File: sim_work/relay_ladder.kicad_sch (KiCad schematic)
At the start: 26 parts, among them Q1 2N3904, Q2 2N3904, Q3 2N3904, Q4 2N3904, SW1 K1, SW2 K2, SW3 K3, SW4 K4

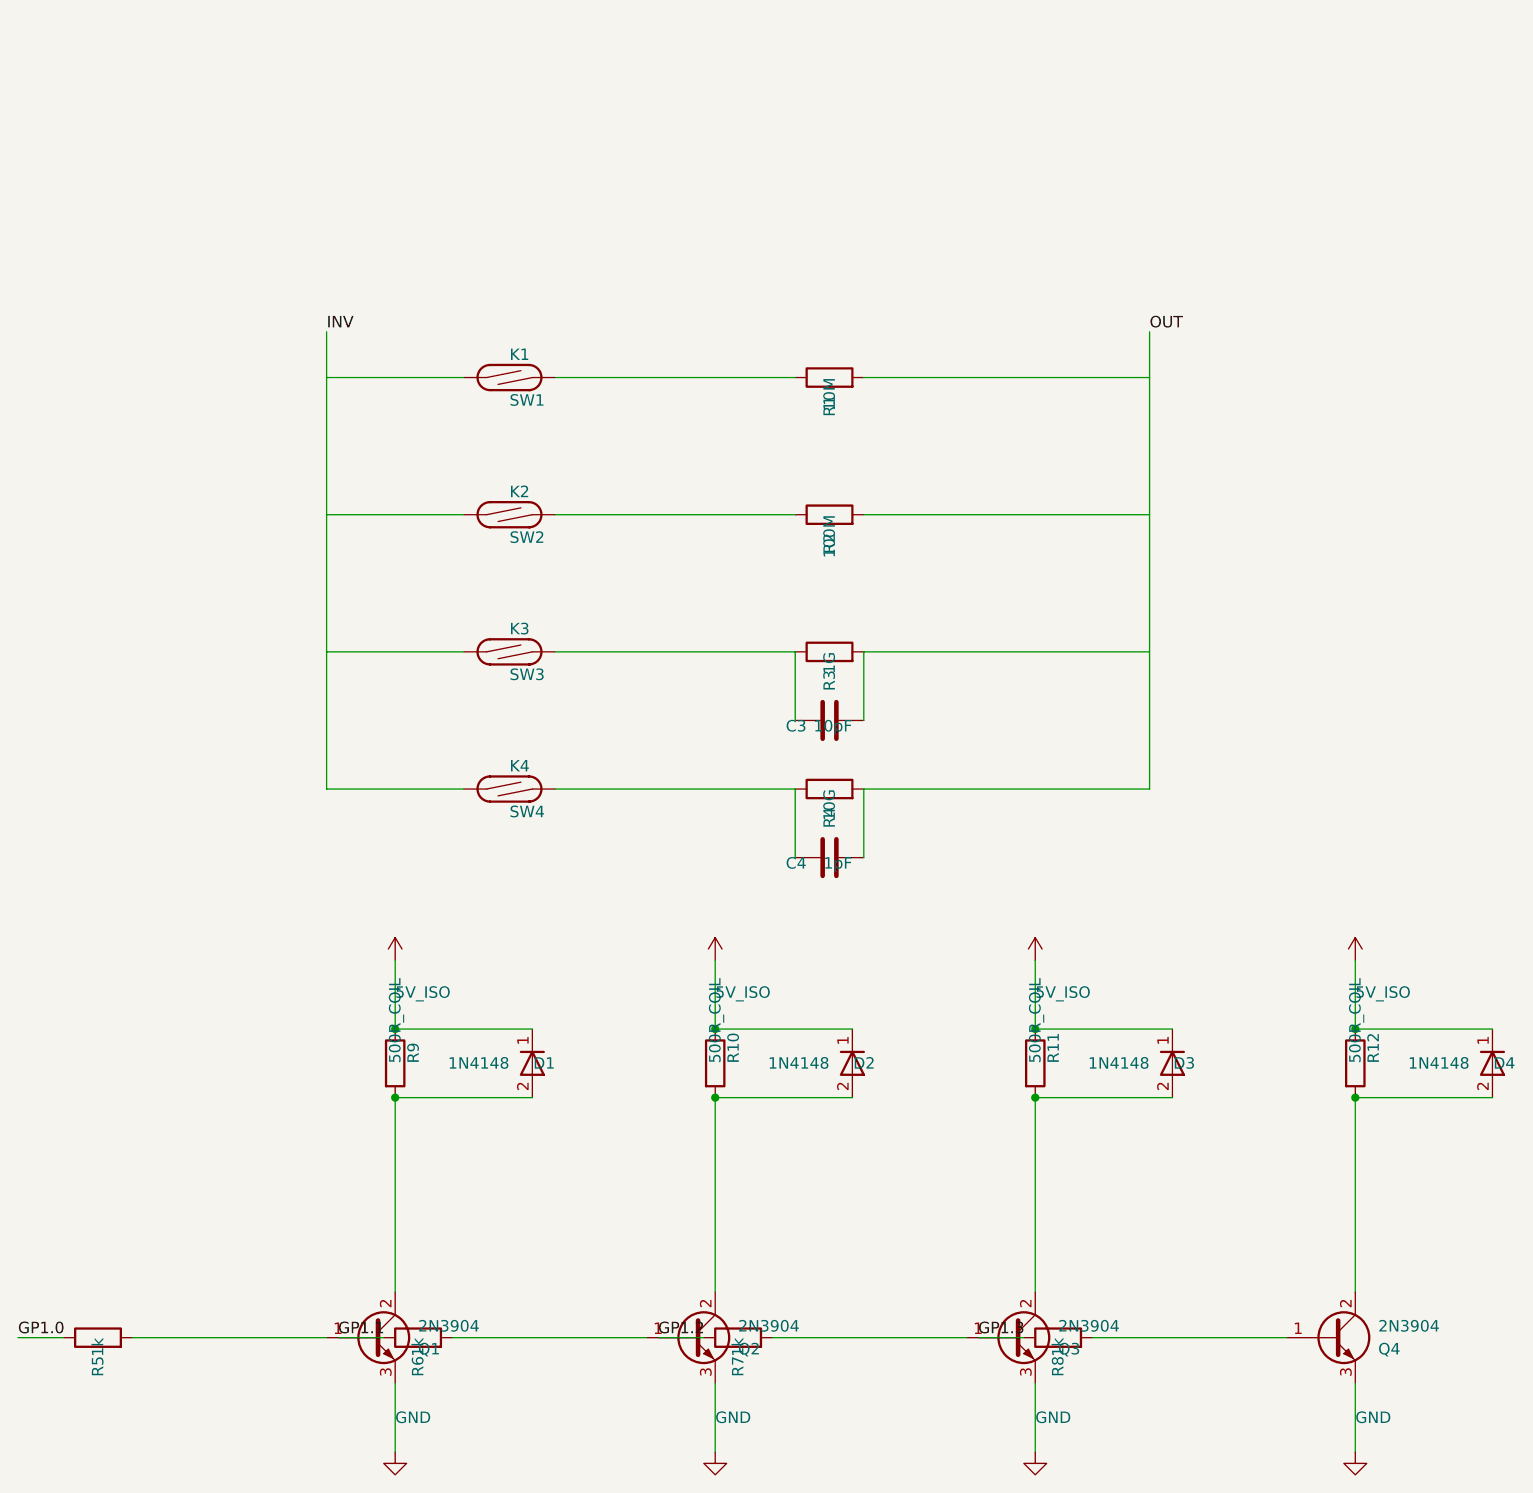
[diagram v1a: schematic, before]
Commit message: Fix schematic connections, add docs and repo portability
- Input filters: R rotation=90 (horizontal), ESD diode rotations fixed,
  junction dots at cathode-signal connection, wires to GND symbols
- Relay ladder: flyback diode rotation 270->90 (K top, A bottom)
- Electrometer/Mux TIA: 4 junction dots each at T-junctions
- AD636 RMS detector: proper IC box with pin labels replaces text-only
- Oscillator blocks: D_Zener symbol, L-shaped cathode routing
- TIA blocks: title/function annotations on all 5 blocks
- New: requirements.txt, docs/oscillator_guide.md
- D_Zener.kicad_sym added to bundled symbols/
- .gitignore updated for docs/ and requirements.txt
- README updated with pip install -r requirements.txt
- PROJECT.md session 9 changelog
- SimGUI builds clean (0 errors)

Co-Authored-By: Claude Opus 4.6 <noreply@anthropic.com>
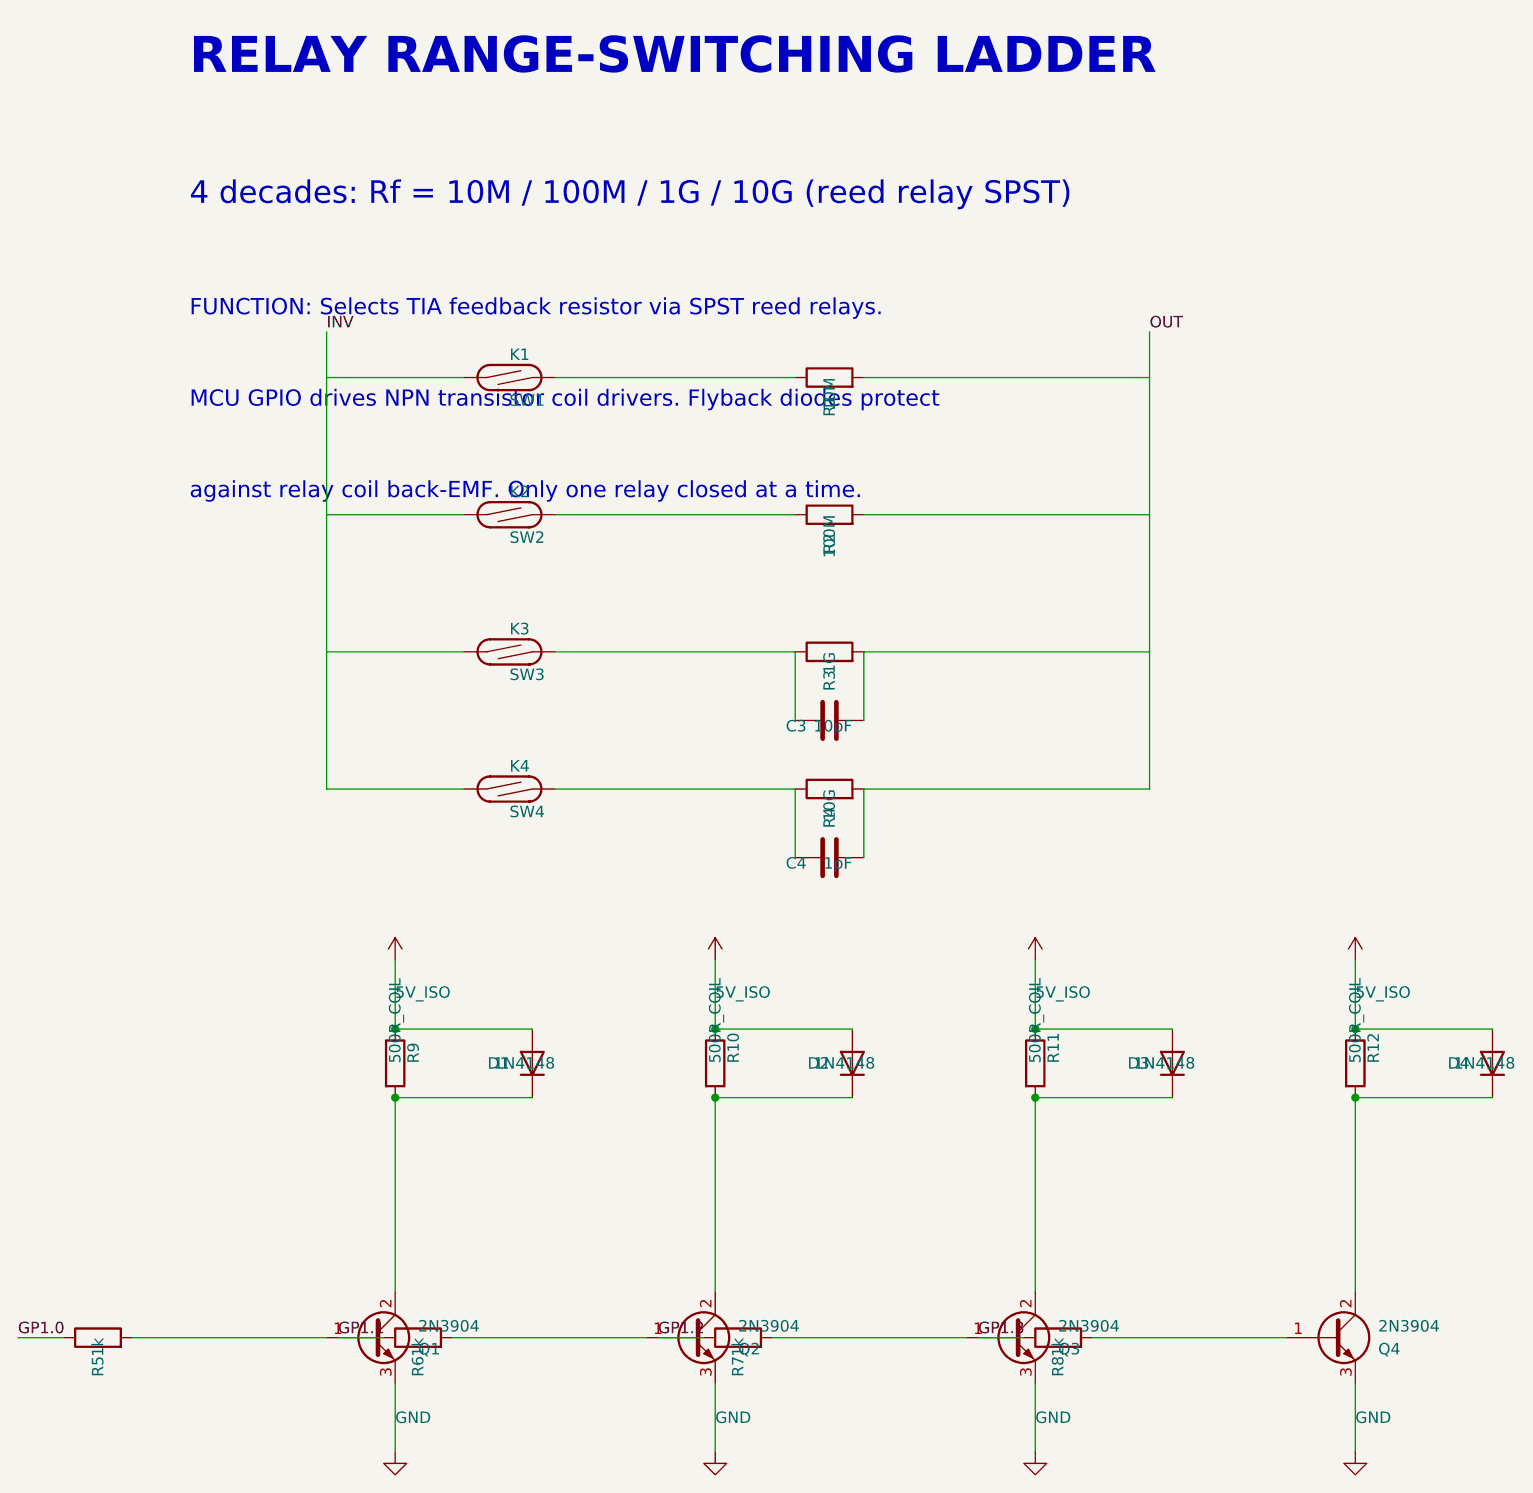
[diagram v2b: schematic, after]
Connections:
- net 5V_ISO: now also D1.2 (A), D2.2 (A), D3.2 (A), D4.2 (A); no longer D1.1 (K), D2.1 (K), D3.1 (K), D4.1 (K)
- net at Q3.2 (C), R11.2: now also D3.1 (K); no longer D3.2 (A)
- net at Q4.2 (C), R12.2: now also D4.1 (K); no longer D4.2 (A)
- net at Q1.2 (C), R9.2: now also D1.1 (K); no longer D1.2 (A)
- net at Q2.2 (C), R10.2: now also D2.1 (K); no longer D2.2 (A)
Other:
- note added: "4 decades: Rf = 10M / 100M / 1G / 10G (reed relay SPST)"
- note added: "FUNCTION: Selects TIA feedback resistor via SPST reed relays."
- note added: "MCU GPIO drives NPN transistor coil drivers. Flyback diodes protect"
- note added: "RELAY RANGE-SWITCHING LADDER"
- note added: "against relay coil back-EMF. Only one relay closed at a time."
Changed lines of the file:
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@@
 		(instances
 			(project "Relay Range Ladder"
-				(path "/fa4591ea-c8c0-4d18-8d69-9ae6b5fcdff9"
+				(path "/435656b3-59c3-4f82-97a8-6813afec584c"
 					(reference "SW1")
 					(unit 1)
@@
 		(instances
 			(project "Relay Range Ladder"
-				(path "/fa4591ea-c8c0-4d18-8d69-9ae6b5fcdff9"
+				(path "/435656b3-59c3-4f82-97a8-6813afec584c"
 					(reference "R1")
 					(unit 1)
@@
 		(instances
 			(project "Relay Range Ladder"
-				(path "/fa4591ea-c8c0-4d18-8d69-9ae6b5fcdff9"
+				(path "/435656b3-59c3-4f82-97a8-6813afec584c"
 					(reference "SW2")
 					(unit 1)
@@
 		(instances
 			(project "Relay Range Ladder"
-				(path "/fa4591ea-c8c0-4d18-8d69-9ae6b5fcdff9"
+				(path "/435656b3-59c3-4f82-97a8-6813afec584c"
 					(reference "R2")
 					(unit 1)
@@
 		(instances
 			(project "Relay Range Ladder"
-				(path "/fa4591ea-c8c0-4d18-8d69-9ae6b5fcdff9"
+				(path "/435656b3-59c3-4f82-97a8-6813afec584c"
 					(reference "SW3")
 					(unit 1)
@@
 		(instances
 			(project "Relay Range Ladder"
-				(path "/fa4591ea-c8c0-4d18-8d69-9ae6b5fcdff9"
+				(path "/435656b3-59c3-4f82-97a8-6813afec584c"
 					(reference "R3")
 					(unit 1)
@@
 		(instances
 			(project "Relay Range Ladder"
-				(path "/fa4591ea-c8c0-4d18-8d69-9ae6b5fcdff9"
+				(path "/435656b3-59c3-4f82-97a8-6813afec584c"
 					(reference "C3")
 					(unit 1)
@@
 		(instances
 			(project "Relay Range Ladder"
-				(path "/fa4591ea-c8c0-4d18-8d69-9ae6b5fcdff9"
+				(path "/435656b3-59c3-4f82-97a8-6813afec584c"
 					(reference "SW4")
 					(unit 1)
@@
 		(instances
 			(project "Relay Range Ladder"
-				(path "/fa4591ea-c8c0-4d18-8d69-9ae6b5fcdff9"
+				(path "/435656b3-59c3-4f82-97a8-6813afec584c"
 					(reference "R4")
 					(unit 1)
@@
 		(instances
 			(project "Relay Range Ladder"
-				(path "/fa4591ea-c8c0-4d18-8d69-9ae6b5fcdff9"
+				(path "/435656b3-59c3-4f82-97a8-6813afec584c"
 					(reference "C4")
 					(unit 1)
@@
 		(instances
 			(project "Relay Range Ladder"
-				(path "/fa4591ea-c8c0-4d18-8d69-9ae6b5fcdff9"
+				(path "/435656b3-59c3-4f82-97a8-6813afec584c"
 					(reference "Q1")
 					(unit 1)
@@
 		(instances
 			(project "Relay Range Ladder"
-				(path "/fa4591ea-c8c0-4d18-8d69-9ae6b5fcdff9"
+				(path "/435656b3-59c3-4f82-97a8-6813afec584c"
 					(reference "R9")
 					(unit 1)
@@
 	(symbol
 		(lib_id "D:D")
-		(at 58.42 127 270)
+		(at 58.42 127 90)
 		(unit 1)
 		(exclude_from_sim no)
@@
 		(fields_autoplaced no)
 		(property "Reference" "D1"
-			(at 60.96 127 270)
+			(at 55.88 127 90)
 			(effects
 				(font
@@
 		)
 		(property "Value" "1N4148"
-			(at 55.88 127 270)
-			(effects
-				(font
-					(size 1.27 1.27)
-				)
-				(justify left)
-			)
-		)
-		(pin "1"
-		)
-		(pin "2"
-		)
-		(instances
-			(project "Relay Range Ladder"
-				(path "/fa4591ea-c8c0-4d18-8d69-9ae6b5fcdff9"
+			(at 60.96 127 90)
+			(effects
+				(font
+					(size 1.27 1.27)
+				)
+				(justify left)
+			)
+		)
+		(pin "1"
+		)
+		(pin "2"
+		)
+		(instances
+			(project "Relay Range Ladder"
+				(path "/435656b3-59c3-4f82-97a8-6813afec584c"
 					(reference "D1")
 					(unit 1)
@@
 		(instances
 			(project "Relay Range Ladder"
-				(path "/fa4591ea-c8c0-4d18-8d69-9ae6b5fcdff9"
+				(path "/435656b3-59c3-4f82-97a8-6813afec584c"
 					(reference "#PWR01")
 					(unit 1)
@@
 		(instances
 			(project "Relay Range Ladder"
-				(path "/fa4591ea-c8c0-4d18-8d69-9ae6b5fcdff9"
+				(path "/435656b3-59c3-4f82-97a8-6813afec584c"
 					(reference "#PWR02")
 					(unit 1)
@@
 		(instances
 			(project "Relay Range Ladder"
-				(path "/fa4591ea-c8c0-4d18-8d69-9ae6b5fcdff9"
+				(path "/435656b3-59c3-4f82-97a8-6813afec584c"
 					(reference "R5")
 					(unit 1)
@@
 		(instances
 			(project "Relay Range Ladder"
-				(path "/fa4591ea-c8c0-4d18-8d69-9ae6b5fcdff9"
+				(path "/435656b3-59c3-4f82-97a8-6813afec584c"
 					(reference "Q2")
 					(unit 1)
@@
 		(instances
 			(project "Relay Range Ladder"
-				(path "/fa4591ea-c8c0-4d18-8d69-9ae6b5fcdff9"
+				(path "/435656b3-59c3-4f82-97a8-6813afec584c"
 					(reference "R10")
 					(unit 1)
@@
 	(symbol
 		(lib_id "D:D")
-		(at 93.98 127 270)
+		(at 93.98 127 90)
 		(unit 1)
 		(exclude_from_sim no)
@@
 		(fields_autoplaced no)
 		(property "Reference" "D2"
-			(at 96.52 127 270)
+			(at 91.44 127 90)
 			(effects
 				(font
@@
 		)
 		(property "Value" "1N4148"
-			(at 91.44 127 270)
-			(effects
-				(font
-					(size 1.27 1.27)
-				)
-				(justify left)
-			)
-		)
-		(pin "1"
-		)
-		(pin "2"
-		)
-		(instances
-			(project "Relay Range Ladder"
-				(path "/fa4591ea-c8c0-4d18-8d69-9ae6b5fcdff9"
+			(at 96.52 127 90)
+			(effects
+				(font
+					(size 1.27 1.27)
+				)
+				(justify left)
+			)
+		)
+		(pin "1"
+		)
+		(pin "2"
+		)
+		(instances
+			(project "Relay Range Ladder"
+				(path "/435656b3-59c3-4f82-97a8-6813afec584c"
 					(reference "D2")
 					(unit 1)
@@
 		(instances
 			(project "Relay Range Ladder"
-				(path "/fa4591ea-c8c0-4d18-8d69-9ae6b5fcdff9"
+				(path "/435656b3-59c3-4f82-97a8-6813afec584c"
 					(reference "#PWR03")
 					(unit 1)
@@
 		(instances
 			(project "Relay Range Ladder"
-				(path "/fa4591ea-c8c0-4d18-8d69-9ae6b5fcdff9"
+				(path "/435656b3-59c3-4f82-97a8-6813afec584c"
 					(reference "#PWR04")
 					(unit 1)
@@
 		(instances
 			(project "Relay Range Ladder"
-				(path "/fa4591ea-c8c0-4d18-8d69-9ae6b5fcdff9"
+				(path "/435656b3-59c3-4f82-97a8-6813afec584c"
 					(reference "R6")
 					(unit 1)
@@
 		(instances
 			(project "Relay Range Ladder"
-				(path "/fa4591ea-c8c0-4d18-8d69-9ae6b5fcdff9"
+				(path "/435656b3-59c3-4f82-97a8-6813afec584c"
 					(reference "Q3")
 					(unit 1)
@@
 		(instances
 			(project "Relay Range Ladder"
-				(path "/fa4591ea-c8c0-4d18-8d69-9ae6b5fcdff9"
+				(path "/435656b3-59c3-4f82-97a8-6813afec584c"
 					(reference "R11")
 					(unit 1)
@@
 	(symbol
 		(lib_id "D:D")
-		(at 129.54 127 270)
+		(at 129.54 127 90)
 		(unit 1)
 		(exclude_from_sim no)
@@
 		(fields_autoplaced no)
 		(property "Reference" "D3"
-			(at 132.08 127 270)
+			(at 127 127 90)
 			(effects
 				(font
@@
 		)
 		(property "Value" "1N4148"
-			(at 127 127 270)
-			(effects
-				(font
-					(size 1.27 1.27)
-				)
-				(justify left)
-			)
-		)
-		(pin "1"
-		)
-		(pin "2"
-		)
-		(instances
-			(project "Relay Range Ladder"
-				(path "/fa4591ea-c8c0-4d18-8d69-9ae6b5fcdff9"
+			(at 132.08 127 90)
+			(effects
+				(font
+					(size 1.27 1.27)
+				)
+				(justify left)
+			)
+		)
+		(pin "1"
+		)
+		(pin "2"
+		)
+		(instances
+			(project "Relay Range Ladder"
+				(path "/435656b3-59c3-4f82-97a8-6813afec584c"
 					(reference "D3")
 					(unit 1)
@@
 		(instances
 			(project "Relay Range Ladder"
-				(path "/fa4591ea-c8c0-4d18-8d69-9ae6b5fcdff9"
+				(path "/435656b3-59c3-4f82-97a8-6813afec584c"
 					(reference "#PWR05")
 					(unit 1)
@@
 		(instances
 			(project "Relay Range Ladder"
-				(path "/fa4591ea-c8c0-4d18-8d69-9ae6b5fcdff9"
+				(path "/435656b3-59c3-4f82-97a8-6813afec584c"
 					(reference "#PWR06")
 					(unit 1)
@@
 		(instances
 			(project "Relay Range Ladder"
-				(path "/fa4591ea-c8c0-4d18-8d69-9ae6b5fcdff9"
+				(path "/435656b3-59c3-4f82-97a8-6813afec584c"
 					(reference "R7")
 					(unit 1)
@@
 		(instances
 			(project "Relay Range Ladder"
-				(path "/fa4591ea-c8c0-4d18-8d69-9ae6b5fcdff9"
+				(path "/435656b3-59c3-4f82-97a8-6813afec584c"
 					(reference "Q4")
 					(unit 1)
@@
 		(instances
 			(project "Relay Range Ladder"
-				(path "/fa4591ea-c8c0-4d18-8d69-9ae6b5fcdff9"
+				(path "/435656b3-59c3-4f82-97a8-6813afec584c"
 					(reference "R12")
 					(unit 1)
@@
 	(symbol
 		(lib_id "D:D")
-		(at 165.1 127 270)
+		(at 165.1 127 90)
 		(unit 1)
 		(exclude_from_sim no)
@@
 		(fields_autoplaced no)
 		(property "Reference" "D4"
-			(at 167.64 127 270)
+			(at 162.56 127 90)
 			(effects
 				(font
@@
 		)
 		(property "Value" "1N4148"
-			(at 162.56 127 270)
-			(effects
-				(font
-					(size 1.27 1.27)
-				)
-				(justify left)
-			)
-		)
-		(pin "1"
-		)
-		(pin "2"
-		)
-		(instances
-			(project "Relay Range Ladder"
-				(path "/fa4591ea-c8c0-4d18-8d69-9ae6b5fcdff9"
+			(at 167.64 127 90)
+			(effects
+				(font
+					(size 1.27 1.27)
+				)
+				(justify left)
+			)
+		)
+		(pin "1"
+		)
+		(pin "2"
+		)
+		(instances
+			(project "Relay Range Ladder"
+				(path "/435656b3-59c3-4f82-97a8-6813afec584c"
 					(reference "D4")
 					(unit 1)
@@
 		(instances
 			(project "Relay Range Ladder"
-				(path "/fa4591ea-c8c0-4d18-8d69-9ae6b5fcdff9"
+				(path "/435656b3-59c3-4f82-97a8-6813afec584c"
 					(reference "#PWR07")
 					(unit 1)
@@
 		(instances
 			(project "Relay Range Ladder"
-				(path "/fa4591ea-c8c0-4d18-8d69-9ae6b5fcdff9"
+				(path "/435656b3-59c3-4f82-97a8-6813afec584c"
 					(reference "#PWR08")
 					(unit 1)
@@
 		(instances
 			(project "Relay Range Ladder"
-				(path "/fa4591ea-c8c0-4d18-8d69-9ae6b5fcdff9"
+				(path "/435656b3-59c3-4f82-97a8-6813afec584c"
 					(reference "R8")
 					(unit 1)
@@
 		)
 	)
+	(text "RELAY RANGE-SWITCHING LADDER"
+		(exclude_from_sim no)
+		(at 20.32 15.24 0.0000)
+		(effects
+			(font
+				(size 4 4)
+				(bold yes)
+			)
+			(justify left)
+		)
+	)
+	(text "4 decades: Rf = 10M / 100M / 1G / 10G (reed relay SPST)"
+		(exclude_from_sim no)
+		(at 20.32 30.48 0.0000)
+		(effects
+			(font
+				(size 2.5 2.5)
+			)
+			(justify left)
+		)
+	)
+	(text "FUNCTION: Selects TIA feedback resistor via SPST reed relays."
+		(exclude_from_sim no)
+		(at 20.32 43.18 0.0000)
+		(effects
+			(font
+				(size 1.8 1.8)
+			)
+			(justify left)
+		)
+	)
+	(text "MCU GPIO drives NPN transistor coil drivers. Flyback diodes protect"
+		(exclude_from_sim no)
+		(at 20.32 53.34 0.0000)
+		(effects
+			(font
+				(size 1.8 1.8)
+			)
+			(justify left)
+		)
+	)
+	(text "against relay coil back-EMF. Only one relay closed at a time."
+		(exclude_from_sim no)
+		(at 20.32 63.5 0.0000)
+		(effects
+			(font
+				(size 1.8 1.8)
+			)
+			(justify left)
+		)
+	)
